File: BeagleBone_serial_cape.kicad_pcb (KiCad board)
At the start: 2 copper layers, 71.1 x 66 mm, 51 parts, among them J1 DB9, J2 DB9, J3 DB9, J4 DB9, P1 CONN_01X03, P2 CONN_01X03, P5 CONN_01X03, P6 CONN_01X03, P8 CONN_02X23, P9 CONN_02X23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

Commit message: routing pcb add more photos Signed-off-by: Patryk Mezydlo <mezydlo.p@gmail.com>
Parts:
- moved P1 27.9 mm to (149.9, 85.1)
- moved P5 27.9 mm to (149.9, 113.0)
- moved C10 1.80 mm to (149.9, 71.1), turned to 0 degrees
- turned C11 to 0 degrees
- turned C12 to 0 degrees
- turned C7 to 0 degrees
- turned C8 to 0 degrees
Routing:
- net +3V3: track 0.00 -> 112.5 mm
- net Net-(D4-Pad2): track 0.00 -> 61.8 mm
- net Net-(D2-Pad2): track 0.00 -> 44.8 mm
- net Net-(D8-Pad2): track 0.00 -> 34.2 mm
- net Net-(J1-Pad3): track 0.00 -> 33.3 mm, vias 0 -> 1
- net Net-(D3-Pad2): track 0.00 -> 31.8 mm
- net Net-(D6-Pad2): track 0.00 -> 30.4 mm, vias 0 -> 1
- net GND: track 0.00 -> 27.5 mm, vias 0 -> 3
- net Net-(J2-Pad3): track 0.00 -> 27.4 mm, vias 0 -> 1
- net Net-(J4-Pad3): track 0.00 -> 26.3 mm, vias 0 -> 1
- net Net-(D9-Pad2): track 0.00 -> 26.1 mm
- net Net-(J1-Pad2): track 0.00 -> 24.7 mm, vias 0 -> 1
- net Net-(J3-Pad3): track 0.00 -> 24.2 mm, vias 0 -> 1
- net Net-(J2-Pad2): track 0.00 -> 23.9 mm
- net Net-(J3-Pad2): track 0.00 -> 23.4 mm, vias 0 -> 1
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- added copper zone on B.Cu, net GND
- added copper zone on F.Cu, net GND

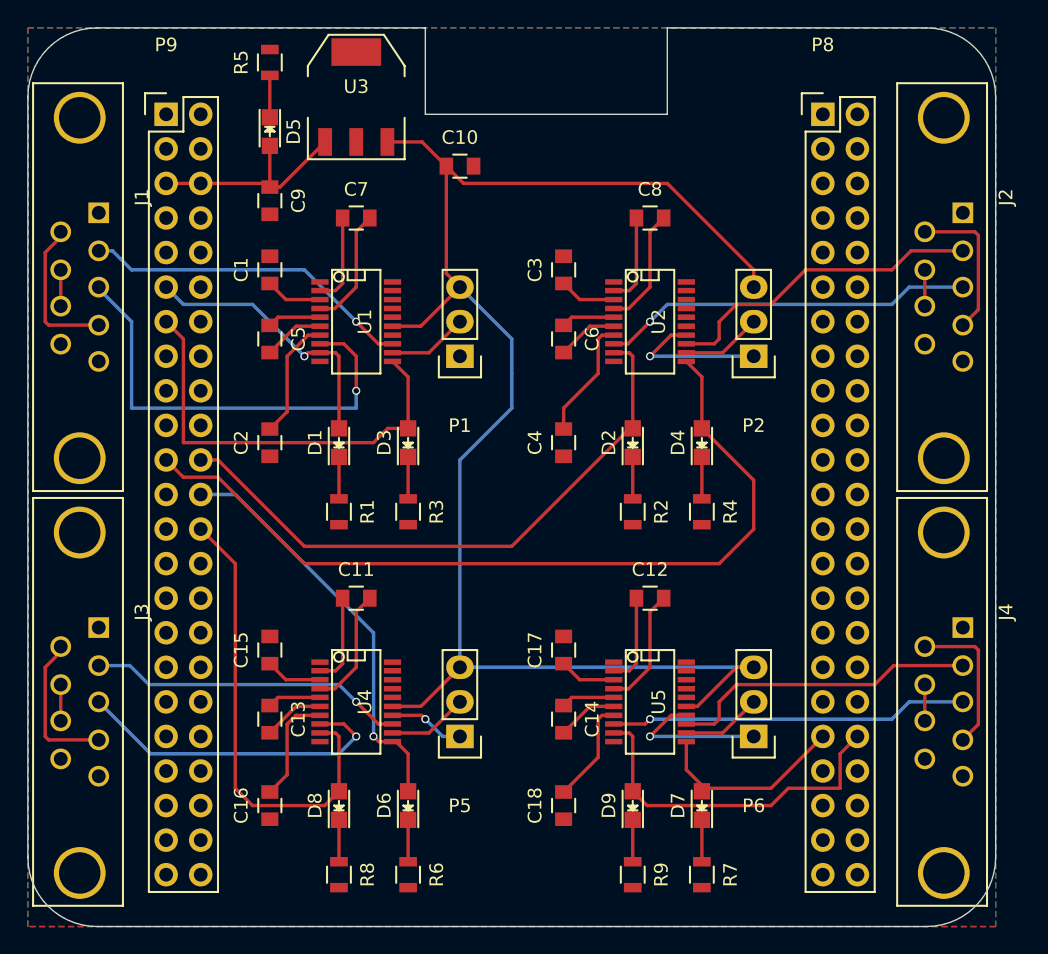
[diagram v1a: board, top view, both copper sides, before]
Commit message: add EEPROM for auto-detect add thicker traces fixed GND and 3.3v routing add bypass capacitors
Signed-off-by: Patryk Mezydlo <mezydlo.p@gmail.com>
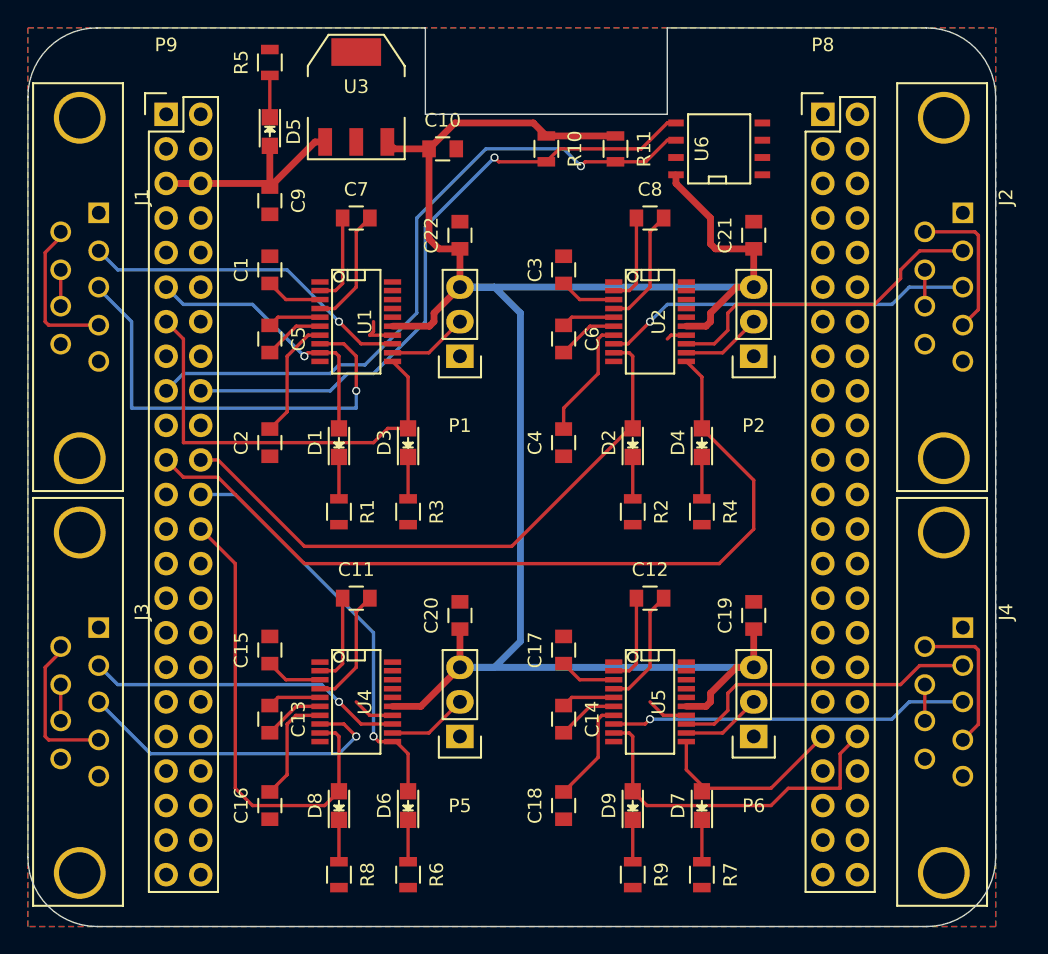
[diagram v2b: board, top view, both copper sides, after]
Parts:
- added C19: 0.1u, Capacitors_SMD:C_0805, F.Cu at (171.4, 104.1)
- added C20: 0.1u, Capacitors_SMD:C_0805, F.Cu at (149.9, 104.1)
- added C21: 0.1u, Capacitors_SMD:C_0805, F.Cu at (171.4, 76.2)
- added C22: 0.1u, Capacitors_SMD:C_0805, F.Cu at (149.9, 76.2)
- added R10: 10k, Resistors_SMD:R_0805, F.Cu at (156.2, 69.8)
- added R11: 10k, Resistors_SMD:R_0805, F.Cu at (161.3, 69.8)
- added U6: 24C512, SMD_Packages:SOIC-8-N, F.Cu at (168.9, 69.8)
- moved C10 1.80 mm to (148.6, 69.8)
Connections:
- J1 pad 1: (no net) -> Net-(J1-Pad1)
- J1 pad 9: (no net) -> Net-(J1-Pad9)
- J2 pad 1: (no net) -> Net-(J2-Pad1)
- J2 pad 9: (no net) -> Net-(J2-Pad9)
- J3 pad 1: (no net) -> Net-(J3-Pad1)
- J3 pad 9: (no net) -> Net-(J3-Pad9)
- J4 pad 1: (no net) -> Net-(J4-Pad1)
- J4 pad 9: (no net) -> Net-(J4-Pad9)
- P8 pad 10: (no net) -> Net-(P8-Pad10)
- P8 pad 11: (no net) -> Net-(P8-Pad11)
- P8 pad 12: (no net) -> Net-(P8-Pad12)
- P8 pad 13: (no net) -> Net-(P8-Pad13)
- P8 pad 14: (no net) -> Net-(P8-Pad14)
- P8 pad 15: (no net) -> Net-(P8-Pad15)
- P8 pad 16: (no net) -> Net-(P8-Pad16)
- P8 pad 17: (no net) -> Net-(P8-Pad17)
- P8 pad 18: (no net) -> Net-(P8-Pad18)
- P8 pad 19: (no net) -> Net-(P8-Pad19)
- P8 pad 20: (no net) -> Net-(P8-Pad20)
- P8 pad 21: (no net) -> Net-(P8-Pad21)
- P8 pad 22: (no net) -> Net-(P8-Pad22)
- P8 pad 23: (no net) -> Net-(P8-Pad23)
- P8 pad 24: (no net) -> Net-(P8-Pad24)
- P8 pad 25: (no net) -> Net-(P8-Pad25)
- P8 pad 26: (no net) -> Net-(P8-Pad26)
- P8 pad 27: (no net) -> Net-(P8-Pad27)
- P8 pad 28: (no net) -> Net-(P8-Pad28)
- P8 pad 29: (no net) -> Net-(P8-Pad29)
- P8 pad 3: (no net) -> Net-(P8-Pad3)
- P8 pad 30: (no net) -> Net-(P8-Pad30)
- P8 pad 31: (no net) -> Net-(P8-Pad31)
- P8 pad 32: (no net) -> Net-(P8-Pad32)
- P8 pad 33: (no net) -> Net-(P8-Pad33)
- P8 pad 34: (no net) -> Net-(P8-Pad34)
- P8 pad 35: (no net) -> Net-(P8-Pad35)
- P8 pad 36: (no net) -> Net-(P8-Pad36)
- P8 pad 39: (no net) -> Net-(P8-Pad39)
- P8 pad 4: (no net) -> Net-(P8-Pad4)
- P8 pad 40: (no net) -> Net-(P8-Pad40)
- P8 pad 41: (no net) -> Net-(P8-Pad41)
- P8 pad 42: (no net) -> Net-(P8-Pad42)
- P8 pad 5: (no net) -> Net-(P8-Pad5)
- P8 pad 6: (no net) -> Net-(P8-Pad6)
- P8 pad 7: (no net) -> Net-(P8-Pad7)
- P8 pad 8: (no net) -> Net-(P8-Pad8)
- P8 pad 9: (no net) -> Net-(P8-Pad9)
- P9 pad 10: (no net) -> Net-(P9-Pad10)
- P9 pad 12: (no net) -> Net-(P9-Pad12)
- P9 pad 14: (no net) -> Net-(P9-Pad14)
- P9 pad 15: (no net) -> Net-(P9-Pad15)
- P9 pad 16: (no net) -> Net-(P9-Pad16)
- P9 pad 17: (no net) -> Net-(P9-Pad17)
- P9 pad 18: (no net) -> Net-(P9-Pad18)
- P9 pad 19: (no net) -> Net-(P9-Pad19)
- P9 pad 20: (no net) -> Net-(P9-Pad20)
- P9 pad 23: (no net) -> Net-(P9-Pad23)
- P9 pad 25: (no net) -> Net-(P9-Pad25)
- P9 pad 27: (no net) -> Net-(P9-Pad27)
- P9 pad 28: (no net) -> Net-(P9-Pad28)
- P9 pad 29: (no net) -> Net-(P9-Pad29)
- P9 pad 3: (no net) -> Net-(P9-Pad3)
- P9 pad 30: (no net) -> Net-(P9-Pad30)
- P9 pad 31: (no net) -> Net-(P9-Pad31)
- P9 pad 32: (no net) -> Net-(P9-Pad32)
- P9 pad 33: (no net) -> Net-(P9-Pad33)
- P9 pad 34: (no net) -> Net-(P9-Pad34)
- P9 pad 35: (no net) -> Net-(P9-Pad35)
- P9 pad 36: (no net) -> Net-(P9-Pad36)
- P9 pad 37: (no net) -> Net-(P9-Pad37)
- P9 pad 38: (no net) -> Net-(P9-Pad38)
- P9 pad 39: (no net) -> Net-(P9-Pad39)
- P9 pad 4: (no net) -> Net-(P9-Pad4)
- P9 pad 40: (no net) -> Net-(P9-Pad40)
- P9 pad 41: (no net) -> Net-(P9-Pad41)
- P9 pad 42: (no net) -> Net-(P9-Pad42)
- P9 pad 7: (no net) -> Net-(P9-Pad7)
- P9 pad 8: (no net) -> Net-(P9-Pad8)
- P9 pad 9: (no net) -> Net-(P9-Pad9)
- U1 pad 1: (no net) -> Net-(U1-Pad1)
- U1 pad 10: (no net) -> Net-(U1-Pad10)
- U1 pad 16: (no net) -> Net-(U1-Pad16)
- U2 pad 1: (no net) -> Net-(U2-Pad1)
- U2 pad 10: (no net) -> Net-(U2-Pad10)
- U2 pad 16: (no net) -> Net-(U2-Pad16)
- U4 pad 1: (no net) -> Net-(U4-Pad1)
- U4 pad 10: (no net) -> Net-(U4-Pad10)
- U4 pad 16: (no net) -> Net-(U4-Pad16)
- U5 pad 1: (no net) -> Net-(U5-Pad1)
- U5 pad 10: (no net) -> Net-(U5-Pad10)
- U5 pad 16: (no net) -> Net-(U5-Pad16)
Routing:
- net Net-(P9-Pad17): track 0.00 -> 50.2 mm, vias 0 -> 1
- net Net-(P9-Pad18): track 0.00 -> 47.4 mm, vias 0 -> 1
- net +3V3: track 112.5 -> 151.8 mm, vias 0 -> 1
- net GND: track 27.5 -> 10.5 mm, vias 3 -> 0
- net VCC: track 16.2 -> 18.9 mm
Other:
- net class POWER_TRACE added: clearance 0.2, trace_width 0.5, via_dia 0.6, via_drill 0.4

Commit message: add bypass capacitor for EEPROM memory
Signed-off-by: Patryk Mezydlo <mezydlo.p@gmail.com>
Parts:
- added C23: 0.1u, Capacitors_SMD:C_0805, F.Cu at (170.2, 64.8)
- moved U6 1.80 mm to (170.2, 68.6)
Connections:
- J1 pad 1: Net-(J1-Pad1) -> (no net)
- J1 pad 9: Net-(J1-Pad9) -> (no net)
- J2 pad 1: Net-(J2-Pad1) -> (no net)
- J2 pad 9: Net-(J2-Pad9) -> (no net)
- J3 pad 1: Net-(J3-Pad1) -> (no net)
- J3 pad 9: Net-(J3-Pad9) -> (no net)
- J4 pad 1: Net-(J4-Pad1) -> (no net)
- J4 pad 9: Net-(J4-Pad9) -> (no net)
- P8 pad 10: Net-(P8-Pad10) -> (no net)
- P8 pad 11: Net-(P8-Pad11) -> (no net)
- P8 pad 12: Net-(P8-Pad12) -> (no net)
- P8 pad 13: Net-(P8-Pad13) -> (no net)
- P8 pad 14: Net-(P8-Pad14) -> (no net)
- P8 pad 15: Net-(P8-Pad15) -> (no net)
- P8 pad 16: Net-(P8-Pad16) -> (no net)
- P8 pad 17: Net-(P8-Pad17) -> (no net)
- P8 pad 18: Net-(P8-Pad18) -> (no net)
- P8 pad 19: Net-(P8-Pad19) -> (no net)
- P8 pad 20: Net-(P8-Pad20) -> (no net)
- P8 pad 21: Net-(P8-Pad21) -> (no net)
- P8 pad 22: Net-(P8-Pad22) -> (no net)
- P8 pad 23: Net-(P8-Pad23) -> (no net)
- P8 pad 24: Net-(P8-Pad24) -> (no net)
- P8 pad 25: Net-(P8-Pad25) -> (no net)
- P8 pad 26: Net-(P8-Pad26) -> (no net)
- P8 pad 27: Net-(P8-Pad27) -> (no net)
- P8 pad 28: Net-(P8-Pad28) -> (no net)
- P8 pad 29: Net-(P8-Pad29) -> (no net)
- P8 pad 3: Net-(P8-Pad3) -> (no net)
- P8 pad 30: Net-(P8-Pad30) -> (no net)
- P8 pad 31: Net-(P8-Pad31) -> (no net)
- P8 pad 32: Net-(P8-Pad32) -> (no net)
- P8 pad 33: Net-(P8-Pad33) -> (no net)
- P8 pad 34: Net-(P8-Pad34) -> (no net)
- P8 pad 35: Net-(P8-Pad35) -> (no net)
- P8 pad 36: Net-(P8-Pad36) -> (no net)
- P8 pad 39: Net-(P8-Pad39) -> (no net)
- P8 pad 4: Net-(P8-Pad4) -> (no net)
- P8 pad 40: Net-(P8-Pad40) -> (no net)
- P8 pad 41: Net-(P8-Pad41) -> (no net)
- P8 pad 42: Net-(P8-Pad42) -> (no net)
- P8 pad 5: Net-(P8-Pad5) -> (no net)
- P8 pad 6: Net-(P8-Pad6) -> (no net)
- P8 pad 7: Net-(P8-Pad7) -> (no net)
- P8 pad 8: Net-(P8-Pad8) -> (no net)
- P8 pad 9: Net-(P8-Pad9) -> (no net)
- P9 pad 10: Net-(P9-Pad10) -> (no net)
- P9 pad 12: Net-(P9-Pad12) -> (no net)
- P9 pad 14: Net-(P9-Pad14) -> (no net)
- P9 pad 15: Net-(P9-Pad15) -> (no net)
- P9 pad 16: Net-(P9-Pad16) -> (no net)
- P9 pad 19: Net-(P9-Pad19) -> (no net)
- P9 pad 20: Net-(P9-Pad20) -> (no net)
- P9 pad 23: Net-(P9-Pad23) -> (no net)
- P9 pad 25: Net-(P9-Pad25) -> (no net)
- P9 pad 27: Net-(P9-Pad27) -> (no net)
- P9 pad 28: Net-(P9-Pad28) -> (no net)
- P9 pad 29: Net-(P9-Pad29) -> (no net)
- P9 pad 3: Net-(P9-Pad3) -> (no net)
- P9 pad 30: Net-(P9-Pad30) -> (no net)
- P9 pad 31: Net-(P9-Pad31) -> (no net)
- P9 pad 32: Net-(P9-Pad32) -> (no net)
- P9 pad 33: Net-(P9-Pad33) -> (no net)
- P9 pad 34: Net-(P9-Pad34) -> (no net)
- P9 pad 35: Net-(P9-Pad35) -> (no net)
- P9 pad 36: Net-(P9-Pad36) -> (no net)
- P9 pad 37: Net-(P9-Pad37) -> (no net)
- P9 pad 38: Net-(P9-Pad38) -> (no net)
- P9 pad 39: Net-(P9-Pad39) -> (no net)
- P9 pad 4: Net-(P9-Pad4) -> (no net)
- P9 pad 40: Net-(P9-Pad40) -> (no net)
- P9 pad 41: Net-(P9-Pad41) -> (no net)
- P9 pad 42: Net-(P9-Pad42) -> (no net)
- P9 pad 7: Net-(P9-Pad7) -> (no net)
- P9 pad 8: Net-(P9-Pad8) -> (no net)
- P9 pad 9: Net-(P9-Pad9) -> (no net)
- U1 pad 1: Net-(U1-Pad1) -> (no net)
- U1 pad 10: Net-(U1-Pad10) -> (no net)
- U1 pad 16: Net-(U1-Pad16) -> (no net)
- U2 pad 1: Net-(U2-Pad1) -> (no net)
- U2 pad 10: Net-(U2-Pad10) -> (no net)
- U2 pad 16: Net-(U2-Pad16) -> (no net)
- U4 pad 1: Net-(U4-Pad1) -> (no net)
- U4 pad 10: Net-(U4-Pad10) -> (no net)
- U4 pad 16: Net-(U4-Pad16) -> (no net)
- U5 pad 1: Net-(U5-Pad1) -> (no net)
- U5 pad 10: Net-(U5-Pad10) -> (no net)
- U5 pad 16: Net-(U5-Pad16) -> (no net)
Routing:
- net +3V3: track 151.8 -> 180.2 mm
- net GND: track 10.5 -> 14.8 mm
- net Net-(P9-Pad17): track 50.2 -> 52.0 mm
- net Net-(P9-Pad18): track 47.4 -> 49.2 mm
